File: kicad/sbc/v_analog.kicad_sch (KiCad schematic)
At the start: 30 parts, among them J2 RGB, J4 S-VIDEO, U12 cxa2075M, X1 OSC

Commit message: moved all symbols into custom library
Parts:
- C15, C16, C18, C19, C25: symbol Device:C -> steckschwein:C
- C17, C23: footprint Capacitor_THT:CP_Radial_D5.0mm_P2.50mm -> Capacitor_THT:CP_Radial_D10.0mm_P5.00mm; symbol Device:C_Polarized -> steckschwein:C_Polarized
- C20, C21, C22, C24, C26, C27: footprint Capacitor_THT:CP_Radial_D6.3mm_P2.50mm -> Capacitor_THT:CP_Radial_D10.0mm_P5.00mm; symbol Device:C_Polarized -> steckschwein:C_Polarized
- J2: symbol Connector:DIN-8 -> steckschwein:DIN-8
- J4: symbol Connector:Mini-DIN-4 -> steckschwein:Mini-DIN-4
- R10, R11, R12, R13, R14, R15, R16, R17, R18, R19, R7, R8, R9: symbol Device:R -> steckschwein:R
- U12: symbol tms99x:cxa2075M -> steckschwein:cxa2075M
- X1: symbol osc:OSC -> steckschwein:OSC

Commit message: moved all footprints into local library
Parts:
- C15, C16, C18, C19, C25: footprint Capacitor_SMD:C_1206_3216Metric_Pad1.33x1.80mm_HandSolder -> steckschwein:C_1206_3216Metric_Pad1.33x1.80mm_HandSolder
- C17, C23: footprint Capacitor_THT:CP_Radial_D10.0mm_P5.00mm -> steckschwein:CP_Radial_D5.0mm_P2.50mm
- C20, C21, C22, C24, C26, C27: footprint Capacitor_THT:CP_Radial_D10.0mm_P5.00mm -> steckschwein:CP_Radial_D6.3mm_P2.50mm
- J2: footprint DIN:DIN-8 -> steckschwein:DIN-8
- J4: footprint minidin:Mini_DIN_4_TE_Connectivity -> steckschwein:Mini_DIN_4_TE_Connectivity
- R10, R11, R12, R13, R14, R15, R16, R17, R18, R19, R7, R8, R9: footprint Resistor_THT:R_Axial_DIN0204_L3.6mm_D1.6mm_P5.08mm_Horizontal -> steckschwein:R_Axial_DIN0204_L3.6mm_D1.6mm_P7.62mm_Horizontal
- U12: footprint Package_SO:SOIC-24W_7.5x15.4mm_P1.27mm -> steckschwein:SOIC-24W_7.5x15.4mm_P1.27mm
- X1: footprint Oscillator:Oscillator_DIP-14_LargePads -> steckschwein:Oscillator_DIP-14_LargePads
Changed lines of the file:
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@@
       (effects (font (size 1.778 1.778)))
     )
-    (property "Footprint" "Oscillator:Oscillator_DIP-14_LargePads" (at 87.63 96.52 0)
+    (property "Footprint" "steckschwein:Oscillator_DIP-14_LargePads" (at 87.63 96.52 0)
       (effects (font (size 1.524 1.524)) hide)
     )
@@
       (effects (font (size 1.016 1.016)))
     )
-    (property "Footprint" "Resistor_THT:R_Axial_DIN0204_L3.6mm_D1.6mm_P5.08mm_Horizontal" (at 165.1 84.328 90)
+    (property "Footprint" "steckschwein:R_Axial_DIN0204_L3.6mm_D1.6mm_P7.62mm_Horizontal" (at 165.1 84.328 90)
       (effects (font (size 0.762 0.762)) hide)
     )
@@
       (effects (font (size 1.016 1.016)))
     )
-    (property "Footprint" "Resistor_THT:R_Axial_DIN0204_L3.6mm_D1.6mm_P5.08mm_Horizontal" (at 165.1 91.948 90)
+    (property "Footprint" "steckschwein:R_Axial_DIN0204_L3.6mm_D1.6mm_P7.62mm_Horizontal" (at 165.1 91.948 90)
       (effects (font (size 0.762 0.762)) hide)
     )
@@
       (effects (font (size 1.016 1.016)))
     )
-    (property "Footprint" "Resistor_THT:R_Axial_DIN0204_L3.6mm_D1.6mm_P5.08mm_Horizontal" (at 115.57 94.488 90)
+    (property "Footprint" "steckschwein:R_Axial_DIN0204_L3.6mm_D1.6mm_P7.62mm_Horizontal" (at 115.57 94.488 90)
       (effects (font (size 0.762 0.762)) hide)
     )
@@
       (effects (font (size 1.27 1.27)) (justify left))
     )
-    (property "Footprint" "Capacitor_SMD:C_1206_3216Metric_Pad1.33x1.80mm_HandSolder" (at 116.5352 77.47 0)
+    (property "Footprint" "steckschwein:C_1206_3216Metric_Pad1.33x1.80mm_HandSolder" (at 116.5352 77.47 0)
       (effects (font (size 0.762 0.762)) hide)
     )
@@
       (effects (font (size 1.016 1.016)))
     )
-    (property "Footprint" "Resistor_THT:R_Axial_DIN0204_L3.6mm_D1.6mm_P5.08mm_Horizontal" (at 165.1 89.408 90)
+    (property "Footprint" "steckschwein:R_Axial_DIN0204_L3.6mm_D1.6mm_P7.62mm_Horizontal" (at 165.1 89.408 90)
       (effects (font (size 0.762 0.762)) hide)
     )
@@
       (effects (font (size 1.27 1.27)) (justify left))
     )
-    (property "Footprint" "Capacitor_THT:CP_Radial_D10.0mm_P5.00mm" (at 180.0352 111.76 0)
+    (property "Footprint" "steckschwein:CP_Radial_D6.3mm_P2.50mm" (at 180.0352 111.76 0)
       (effects (font (size 1.27 1.27)) hide)
     )
@@
       (effects (font (size 1.524 1.524)))
     )
-    (property "Footprint" "Package_SO:SOIC-24W_7.5x15.4mm_P1.27mm" (at 140.97 110.49 0)
+    (property "Footprint" "steckschwein:SOIC-24W_7.5x15.4mm_P1.27mm" (at 140.97 110.49 0)
       (effects (font (size 1.524 1.524)) hide)
     )
@@
       (effects (font (size 1.016 1.016)))
     )
-    (property "Footprint" "Resistor_THT:R_Axial_DIN0204_L3.6mm_D1.6mm_P5.08mm_Horizontal" (at 105.918 80.01 90)
+    (property "Footprint" "steckschwein:R_Axial_DIN0204_L3.6mm_D1.6mm_P7.62mm_Horizontal" (at 105.918 80.01 90)
       (effects (font (size 0.762 0.762)) hide)
     )
@@
       (effects (font (size 1.016 1.016)))
     )
-    (property "Footprint" "Resistor_THT:R_Axial_DIN0204_L3.6mm_D1.6mm_P5.08mm_Horizontal" (at 193.802 96.52 90)
+    (property "Footprint" "steckschwein:R_Axial_DIN0204_L3.6mm_D1.6mm_P7.62mm_Horizontal" (at 193.802 96.52 90)
       (effects (font (size 0.762 0.762)) hide)
     )
@@
       (effects (font (size 1.016 1.016)))
     )
-    (property "Footprint" "Resistor_THT:R_Axial_DIN0204_L3.6mm_D1.6mm_P5.08mm_Horizontal" (at 165.1 86.868 90)
+    (property "Footprint" "steckschwein:R_Axial_DIN0204_L3.6mm_D1.6mm_P7.62mm_Horizontal" (at 165.1 86.868 90)
       (effects (font (size 0.762 0.762)) hide)
     )
@@
       (effects (font (size 1.27 1.27)) (justify left))
     )
-    (property "Footprint" "Capacitor_THT:CP_Radial_D10.0mm_P5.00mm" (at 173.6852 111.76 0)
+    (property "Footprint" "steckschwein:CP_Radial_D6.3mm_P2.50mm" (at 173.6852 111.76 0)
       (effects (font (size 1.27 1.27)) hide)
     )
@@
       (effects (font (size 1.27 1.27)) (justify left))
     )
-    (property "Footprint" "Capacitor_THT:CP_Radial_D10.0mm_P5.00mm" (at 175.5648 73.66 0)
+    (property "Footprint" "steckschwein:CP_Radial_D6.3mm_P2.50mm" (at 175.5648 73.66 0)
       (effects (font (size 1.27 1.27)) hide)
     )
@@
       (effects (font (size 1.016 1.016)))
     )
-    (property "Footprint" "Resistor_THT:R_Axial_DIN0204_L3.6mm_D1.6mm_P5.08mm_Horizontal" (at 115.57 104.648 90)
+    (property "Footprint" "steckschwein:R_Axial_DIN0204_L3.6mm_D1.6mm_P7.62mm_Horizontal" (at 115.57 104.648 90)
       (effects (font (size 0.762 0.762)) hide)
     )
@@
       (effects (font (size 1.016 1.016)))
     )
-    (property "Footprint" "Resistor_THT:R_Axial_DIN0204_L3.6mm_D1.6mm_P5.08mm_Horizontal" (at 98.298 80.01 90)
+    (property "Footprint" "steckschwein:R_Axial_DIN0204_L3.6mm_D1.6mm_P7.62mm_Horizontal" (at 98.298 80.01 90)
       (effects (font (size 0.762 0.762)) hide)
     )
@@
       (effects (font (size 1.27 1.27)) (justify left))
     )
-    (property "Footprint" "Capacitor_SMD:C_1206_3216Metric_Pad1.33x1.80mm_HandSolder" (at 122.8852 116.84 0)
+    (property "Footprint" "steckschwein:C_1206_3216Metric_Pad1.33x1.80mm_HandSolder" (at 122.8852 116.84 0)
       (effects (font (size 0.762 0.762)) hide)
     )
@@
       (effects (font (size 1.27 1.27)) (justify left))
     )
-    (property "Footprint" "Capacitor_THT:CP_Radial_D10.0mm_P5.00mm" (at 194.6148 73.66 0)
+    (property "Footprint" "steckschwein:CP_Radial_D6.3mm_P2.50mm" (at 194.6148 73.66 0)
       (effects (font (size 1.27 1.27)) hide)
     )
@@
       (effects (font (size 1.016 1.016)))
     )
-    (property "Footprint" "Resistor_THT:R_Axial_DIN0204_L3.6mm_D1.6mm_P5.08mm_Horizontal" (at 165.1 99.568 90)
+    (property "Footprint" "steckschwein:R_Axial_DIN0204_L3.6mm_D1.6mm_P7.62mm_Horizontal" (at 165.1 99.568 90)
       (effects (font (size 0.762 0.762)) hide)
     )
@@
       (effects (font (size 1.27 1.27)) (justify left))
     )
-    (property "Footprint" "Capacitor_THT:CP_Radial_D10.0mm_P5.00mm" (at 116.5352 116.84 0)
+    (property "Footprint" "steckschwein:CP_Radial_D5.0mm_P2.50mm" (at 116.5352 116.84 0)
       (effects (font (size 1.27 1.27)) hide)
     )
@@
       (effects (font (size 1.27 1.27)) (justify left))
     )
-    (property "Footprint" "Capacitor_THT:CP_Radial_D10.0mm_P5.00mm" (at 182.5752 101.6 0)
+    (property "Footprint" "steckschwein:CP_Radial_D5.0mm_P2.50mm" (at 182.5752 101.6 0)
       (effects (font (size 1.27 1.27)) hide)
     )
@@
       (effects (font (size 1.016 1.016)))
     )
-    (property "Footprint" "Resistor_THT:R_Axial_DIN0204_L3.6mm_D1.6mm_P5.08mm_Horizontal" (at 165.1 102.108 90)
+    (property "Footprint" "steckschwein:R_Axial_DIN0204_L3.6mm_D1.6mm_P7.62mm_Horizontal" (at 165.1 102.108 90)
       (effects (font (size 0.762 0.762)) hide)
     )
@@
       (effects (font (size 1.27 1.27)) (justify left))
     )
-    (property "Footprint" "Capacitor_THT:CP_Radial_D10.0mm_P5.00mm" (at 181.9148 73.66 0)
+    (property "Footprint" "steckschwein:CP_Radial_D6.3mm_P2.50mm" (at 181.9148 73.66 0)
       (effects (font (size 1.27 1.27)) hide)
     )
@@
       (effects (font (size 1.016 1.016)))
     )
-    (property "Footprint" "Resistor_THT:R_Axial_DIN0204_L3.6mm_D1.6mm_P5.08mm_Horizontal" (at 165.1 104.648 90)
+    (property "Footprint" "steckschwein:R_Axial_DIN0204_L3.6mm_D1.6mm_P7.62mm_Horizontal" (at 165.1 104.648 90)
       (effects (font (size 0.762 0.762)) hide)
     )
@@
       (effects (font (size 1.27 1.27)) (justify left))
     )
-    (property "Footprint" "Capacitor_SMD:C_1206_3216Metric_Pad1.33x1.80mm_HandSolder" (at 121.6152 77.47 0)
+    (property "Footprint" "steckschwein:C_1206_3216Metric_Pad1.33x1.80mm_HandSolder" (at 121.6152 77.47 0)
       (effects (font (size 0.762 0.762)) hide)
     )
@@
       (effects (font (size 1.27 1.27)) (justify left bottom))
     )
-    (property "Footprint" "minidin:Mini_DIN_4_TE_Connectivity" (at 176.53 146.05 0)
+    (property "Footprint" "steckschwein:Mini_DIN_4_TE_Connectivity" (at 176.53 146.05 0)
       (effects (font (size 1.27 1.27)) hide)
     )
@@
       (effects (font (size 1.27 1.27)) (justify left))
     )
-    (property "Footprint" "DIN:DIN-8" (at 187.96 41.91 0)
+    (property "Footprint" "steckschwein:DIN-8" (at 187.96 41.91 0)
       (effects (font (size 1.27 1.27)) hide)
     )
@@
       (effects (font (size 1.016 1.016)))
     )
-    (property "Footprint" "Resistor_THT:R_Axial_DIN0204_L3.6mm_D1.6mm_P5.08mm_Horizontal" (at 102.108 80.01 90)
+    (property "Footprint" "steckschwein:R_Axial_DIN0204_L3.6mm_D1.6mm_P7.62mm_Horizontal" (at 102.108 80.01 90)
       (effects (font (size 0.762 0.762)) hide)
     )
@@
       (effects (font (size 1.27 1.27)) (justify left))
     )
-    (property "Footprint" "Capacitor_THT:CP_Radial_D10.0mm_P5.00mm" (at 188.2648 73.66 0)
+    (property "Footprint" "steckschwein:CP_Radial_D6.3mm_P2.50mm" (at 188.2648 73.66 0)
       (effects (font (size 1.27 1.27)) hide)
     )
@@
       (effects (font (size 1.27 1.27)) (justify left))
     )
-    (property "Footprint" "Capacitor_SMD:C_1206_3216Metric_Pad1.33x1.80mm_HandSolder" (at 188.9252 101.6 0)
+    (property "Footprint" "steckschwein:C_1206_3216Metric_Pad1.33x1.80mm_HandSolder" (at 188.9252 101.6 0)
       (effects (font (size 0.762 0.762)) hide)
     )
@@
       (effects (font (size 1.27 1.27)) (justify left))
     )
-    (property "Footprint" "Capacitor_SMD:C_1206_3216Metric_Pad1.33x1.80mm_HandSolder" (at 111.4552 77.47 0)
-      (effects (font (size 0.762 0.762)) hide)
-    )
+    (property "Footprint" "steckschwein:C_1206_3216Metric_Pad1.33x1.80mm_HandSolder" (at 111.4552 77.47 0)
+      (effects (font (size 0.762 0.762)) hide)
+    )

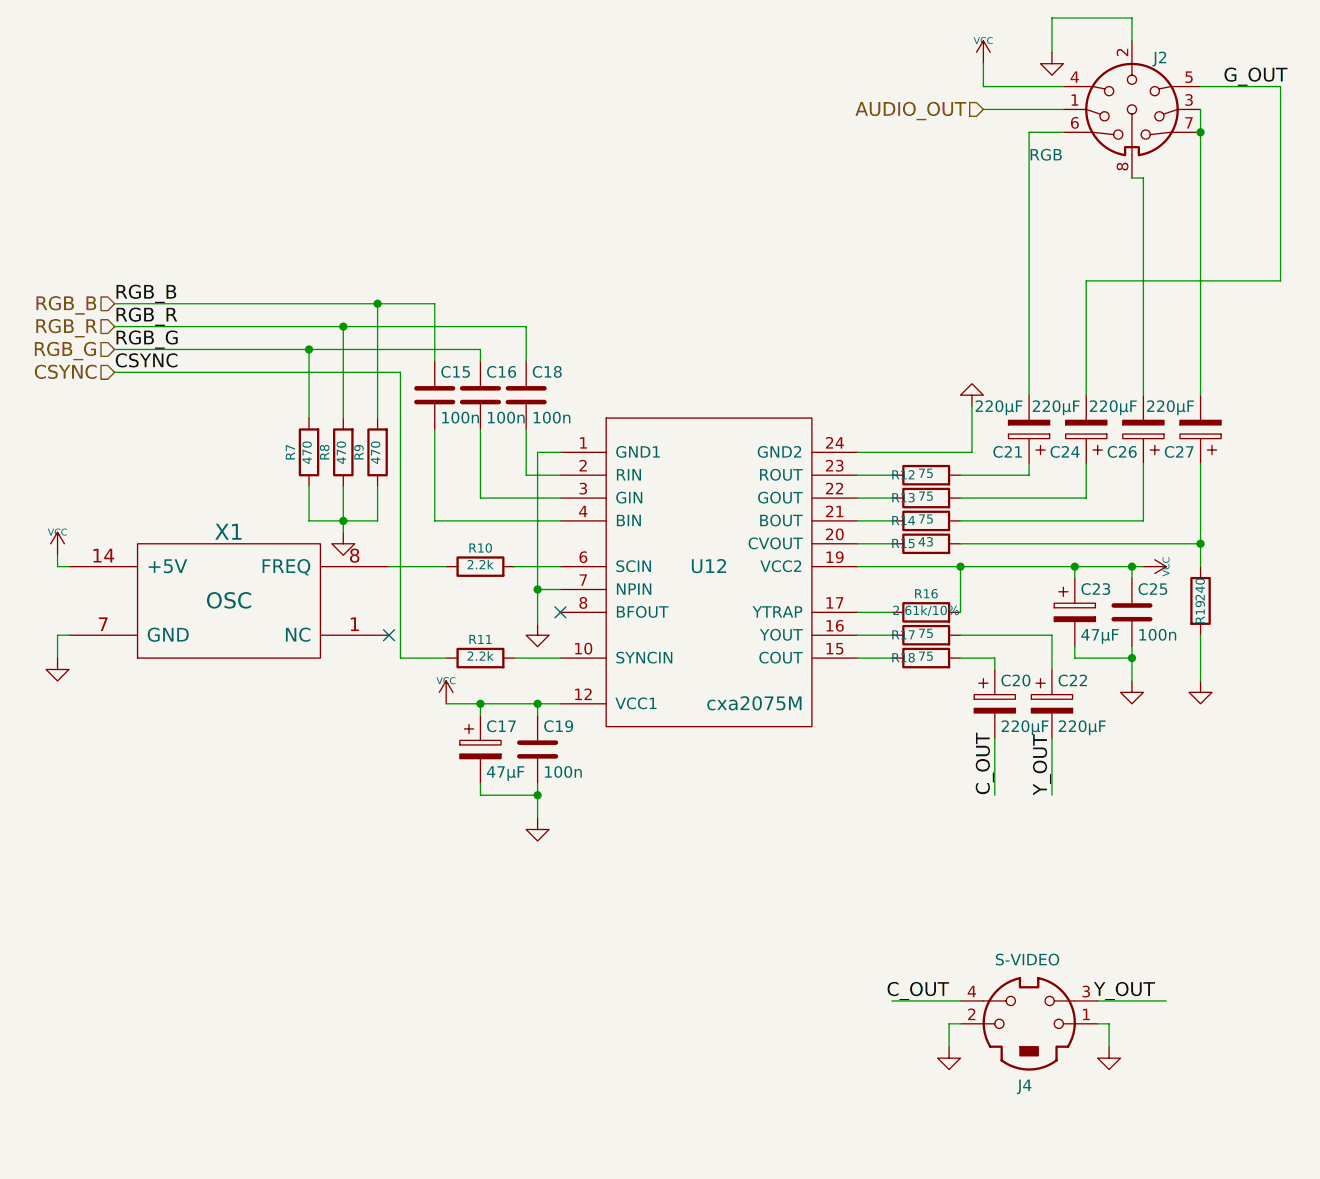
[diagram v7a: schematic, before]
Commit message: component values/units cleanup
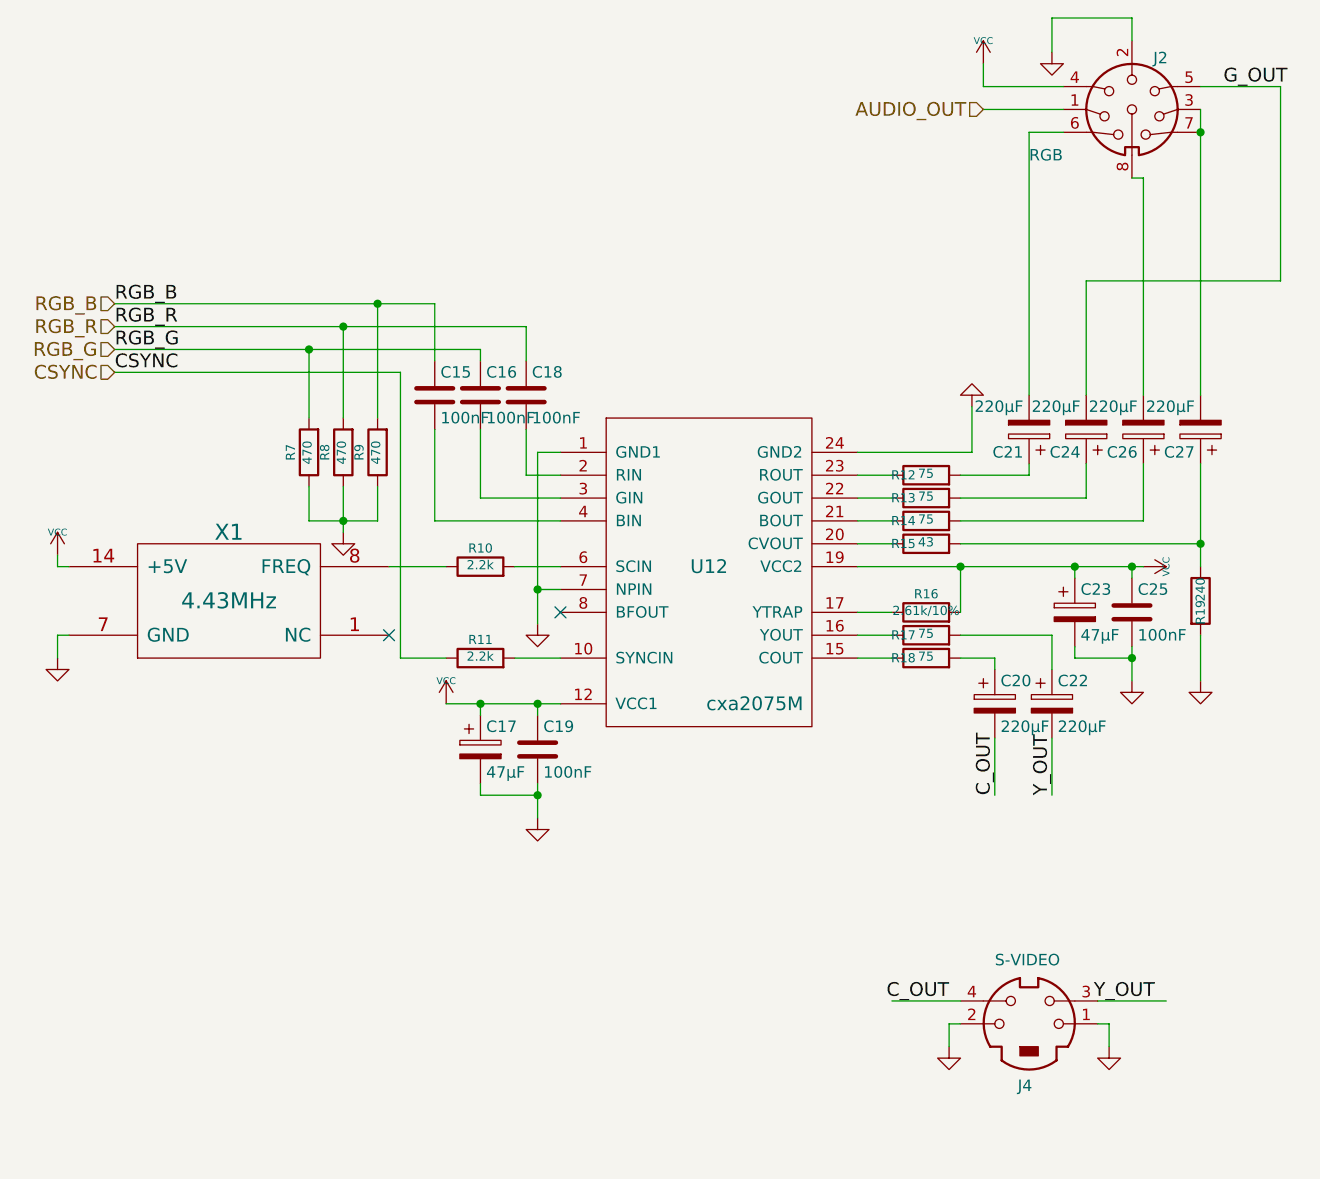
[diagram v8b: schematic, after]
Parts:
- C15, C16, C18, C19, C25: value 100n -> 100nF
- X1: value OSC -> 4.43MHz
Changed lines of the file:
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@@
       (effects (font (size 1.778 1.778)))
     )
-    (property "Value" "OSC" (at 87.63 96.52 0)
+    (property "Value" "4.43MHz" (at 87.63 96.52 0)
       (effects (font (size 1.778 1.778)))
     )
@@
       (effects (font (size 1.27 1.27)) (justify left))
     )
-    (property "Value" "100n" (at 116.205 76.2 0)
+    (property "Value" "100nF" (at 116.205 76.2 0)
       (effects (font (size 1.27 1.27)) (justify left))
     )
@@
       (effects (font (size 1.27 1.27)) (justify left))
     )
-    (property "Value" "100n" (at 122.555 115.57 0)
+    (property "Value" "100nF" (at 122.555 115.57 0)
       (effects (font (size 1.27 1.27)) (justify left))
     )
@@
       (effects (font (size 1.27 1.27)) (justify left))
     )
-    (property "Value" "100n" (at 121.285 76.2 0)
+    (property "Value" "100nF" (at 121.285 76.2 0)
       (effects (font (size 1.27 1.27)) (justify left))
     )
@@
       (effects (font (size 1.27 1.27)) (justify left))
     )
-    (property "Value" "100n" (at 188.595 100.33 0)
+    (property "Value" "100nF" (at 188.595 100.33 0)
       (effects (font (size 1.27 1.27)) (justify left))
     )
@@
       (effects (font (size 1.27 1.27)) (justify left))
     )
-    (property "Value" "100n" (at 111.125 76.2 0)
-      (effects (font (size 1.27 1.27)) (justify left))
-    )
+    (property "Value" "100nF" (at 111.125 76.2 0)
+      (effects (font (size 1.27 1.27)) (justify left))
+    )
